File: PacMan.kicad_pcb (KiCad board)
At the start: 2 copper layers, 139.7 x 117.5 mm, 153 parts, among them J1 POWER+, J10 SEG2 CellMen, J11 SEG1 Balance, J12 SEG2 Balance, J13 AIR Left, J14 AIR Right, J15 SEG1, J16 SEG2, J2 POWER-, J3 TSV IN, J4 Charge Detection, J5 SEG1 CellMen, J6 BusBar Current Sensor, J7 Panel, J8 SLOOP, J9 GLV/CAN, K1 G5Q-1A4 DC24, K2 T9AS1D12-24, K3 T9AS1D12-24, Q1 BSS123, Q2 DMN3730U, Q4 DMP10H4D2S, Q5 DMP10H4D2S, U1 MCP9804, U10 LTC4151, U11 INA592, U12 VIFSD1-S24-S5-SIP, U13 V7805-500, U14 Si8600AC, U15 Si8600AC, U16 TEC3-2419, U17 TEC3-2419, U18 AP2204K-5.0, U19 INA233, U2 TEC2-4815WI, U20 INA233, U3 ADM6320, U4 MCP2551-I-SN, U5 ESP32_DEVKITC, U6 MCP23008, U7 BQ32002, U8 ACHS-7122, U9 PDQE10-Q48-S24-D, Y1 RTC_32K

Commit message: Re-layout to account for the new esp32, put on the RTC, the balancing measurement stuff, pretty much finished up the board, added some comments to schematic and other changes
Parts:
- removed TP1: TSV_RTN, Resistor_SMD:R_0805_2012Metric_Pad1.15x1.40mm_HandSolder
- removed TP2: TSV_5V, TestPoint:TestPoint_Pad_D1.5mm
- C24, C25, C26: footprint Capacitor_SMD:C_0805_2012Metric_Pad1.15x1.40mm_HandSolder -> Capacitor_SMD:C_1206_3216Metric_Pad1.42x1.75mm_HandSolder
- C27: value 4.7uF -> 4.7uF/50V; footprint Capacitor_SMD:C_0805_2012Metric_Pad1.15x1.40mm_HandSolder -> Capacitor_SMD:C_1206_3216Metric_Pad1.42x1.75mm_HandSolder
- C30: value 1u -> 1u/50V
- C32: value 2.2u -> 2.2u/25V
- F1: value Pack+ -> 500mA
- F2: value Pack- -> 500mA
- J11: value SEG1 Balance -> BAL1
- J12: value SEG2 Balance -> BAL2
- Q1: value BSS123 -> DMN3730U
- U12: value VIFSD1-S24-S5-SIP -> MEF1S2405SP3C
- Y1: footprint Crystal:Crystal_SMD_SeikoEpson_MC405-2Pin_9.6x4.1mm_HandSoldering -> Crystal:Crystal_SMD_SeikoEpson_MC405-2Pin_9.6x4.1mm
- moved D7 171.9 mm to (203.2, 106.7), turned to 270 degrees
- moved R41 170.3 mm to (200.7, 106.7), turned to 270 degrees
- moved Q2 162.2 mm to (197.5, 106.7)
- moved Y1 142.5 mm to (116.8, 117.5), turned to 180 degrees
- moved BT1 138.2 mm to (113.7, 124.5), turned to 180 degrees
- moved C34 130.3 mm to (120.7, 127.0), turned to 180 degrees
- moved U7 112.3 mm to (120.7, 123.2)
- moved U5 56.6 mm to (142.9, 130.8)
- moved U20 43.5 mm to (94.6, 49.5), turned to 90 degrees
- moved R37 42.5 mm to (94.6, 42.5), turned to 0 degrees
- moved U19 40.8 mm to (111.1, 49.5), turned to 90 degrees
- moved R36 38.1 mm to (111.1, 42.5), turned to 0 degrees
- moved LOGO2 37.5 mm to (158.1, 40.6)
- moved LOGO1 36.8 mm to (142.9, 43.2)
- moved C33 36.7 mm to (90.8, 52.1)
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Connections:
- net /TSV_5V_AMPS renamed /AMPS_PWR
- C14 pad 2: /PACK_RTN -> /BAL_SEG1-
- C16 pad 1: /PACK_RTN -> /BAL_SEG1-
- C17 pad 2: /PACK_RTN -> /BAL_SEG1-
- C20 pad 2: /SEG2_RTN -> /BAL_SEG2-
- C23 pad 2: /PACK_RTN -> /BAL_SEG1-
- C27 pad 2: /PACK_RTN -> /BAL_SEG1-
- C28 pad 2: /PACK_RTN -> /BAL_SEG1-
- C29 pad 2: /SEG2_RTN -> /BAL_SEG2-
- C30 pad 2: /SEG2_RTN -> /BAL_SEG2-
- C31 pad 1: /PACK_RTN -> /BAL_SEG1-
- C32 pad 2: /SEG2_RTN -> /BAL_SEG2-
- C33 pad 1: /SEG2_RTN -> /BAL_SEG2-
- F2 pad 2: /PACK_RTN -> /BAL_SEG1-
- ISO4 pad 3: /PACK_RTN -> /BAL_SEG1-
- J10 pad 2: /SEG2_RTN -> /BAL_SEG2-
- J10 pad 5: /SEG2_RTN -> /BAL_SEG2-
- J11 pad 1: (no net) -> /BAL_SEG1-
- J11 pad 2: (no net) -> /BAL_SEG1+
- J12 pad 1: (no net) -> /BAL_SEG2-
- J12 pad 2: (no net) -> /BAL_SEG2+
- J15 pad 1: (no net) -> /BAL_SEG1-
- J15 pad 2: (no net) -> /SEG1+
- J16 pad 1: (no net) -> /BAL_SEG2-
- J16 pad 2: (no net) -> /SEG2+
- J5 pad 2: /PACK_RTN -> /BAL_SEG1-
- J5 pad 5: /PACK_RTN -> /BAL_SEG1-
- J6 pad 4: /PACK_RTN -> /BAL_SEG1-
- J7 pad 11: /DISP_BUSY -> /DISP_CS
- J7 pad 13: /DISP_DC -> /DISP_BUSY
- J7 pad 17: /DISP_CS -> /DISP_DC
- R30 pad 1: /PACK_RTN -> /BAL_SEG1-
- R31 pad 1: /PACK_RTN -> /BAL_SEG1-
- R34 pad 2: /PACK_RTN -> /BAL_SEG1-
- R36 pad 1: /Charging/SEG1+ -> /SEG1+
- R36 pad 2: /Charging/BAL_SEG1+ -> /BAL_SEG1+
- R37 pad 1: /Charging/SEG2+ -> /SEG2+
- R37 pad 2: /Charging/BAL_SEG2+ -> /BAL_SEG2+
- TP14 pad 1: /SEG2_RTN -> /BAL_SEG2-
- U10 pad 3: /PACK_RTN -> /BAL_SEG1-
- U10 pad 4: /PACK_RTN -> /BAL_SEG1-
- U10 pad 9: /PACK_RTN -> /BAL_SEG1-
- U11 pad 1: /PACK_RTN -> /BAL_SEG1-
- U11 pad 4: /PACK_RTN -> /BAL_SEG1-
- U12 pad 4: /PACK_RTN -> /BAL_SEG1-
- U14 pad 5: /PACK_RTN -> /BAL_SEG1-
- U15 pad 5: /SEG2_RTN -> /BAL_SEG2-
- U16 pad 7: /PACK_RTN -> /BAL_SEG1-
- U17 pad 7: /SEG2_RTN -> /BAL_SEG2-
- U18 pad 2: /SEG2_RTN -> /BAL_SEG2-
- U19 pad 1: /PACK_RTN -> /BAL_SEG1-
- U19 pad 10: /Charging/BAL_SEG1+ -> /BAL_SEG1+
- U19 pad 2: /PACK_RTN -> /BAL_SEG1-
- U19 pad 7: /PACK_RTN -> /BAL_SEG1-
- U19 pad 8: /Charging/BAL_SEG1+ -> /BAL_SEG1+
- U19 pad 9: /Charging/SEG1+ -> /SEG1+
- U20 pad 1: /SEG2_RTN -> /BAL_SEG2-
- U20 pad 10: /Charging/BAL_SEG2+ -> /BAL_SEG2+
- U20 pad 2: /SEG2_RTN -> /BAL_SEG2-
- U20 pad 7: /SEG2_RTN -> /BAL_SEG2-
- U20 pad 8: /Charging/BAL_SEG2+ -> /BAL_SEG2+
- U20 pad 9: /Charging/SEG2+ -> /SEG2+
- U5 pad 21: (no net) -> /MCU/WATCHDOG
- U5 pad 29: /DISP_BUSY -> (no net)
- U5 pad 3: /MCU/BTN_CENTER_MCU -> /MCU/BTN_LEFT_MCU
- U5 pad 30: /~CHRG_DETECT -> (no net)
- U5 pad 31: /MCU/WATCHDOG -> /DISP_BUSY
- U5 pad 33: (no net) -> /~CHRG_DETECT
- U5 pad 4: /MCU/BTN_UP_MCU -> /MCU/BTN_RIGHT_MCU
- U5 pad 5: /MCU/BTN_DOWN_MCU -> /MCU/BTN_UP_MCU
- U5 pad 6: /MCU/BTN_LEFT_MCU -> /MCU/BTN_DOWN_MCU
- U5 pad 7: /MCU/BTN_RIGHT_MCU -> /MCU/BTN_CENTER_MCU
- U9 pad 1: /PACK_RTN -> /BAL_SEG1-
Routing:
- net /SEG1_5V: track 182.5 -> 227.5 mm
- net /MCU/WATCHDOG: track 81.8 -> 44.8 mm, vias 5 -> 2
- net /BAL_SEG1-: track 0.00 -> 36.2 mm, vias 0 -> 22
- net /LV_3V3: track 277.3 -> 311.1 mm, vias 15 -> 16
- net /LV_24V: track 195.4 -> 226.1 mm
- net /CHRG_EN: track 50.2 -> 20.5 mm
- net /SEG2_5V: track 37.1 -> 65.3 mm
- net /PACK_RTN: track 24.2 -> 0.00 mm, vias 22 -> 0
- net /DISP_CS: track 44.9 -> 60.3 mm, vias 0 -> 2
- net /CHRG_LED: track 68.7 -> 82.5 mm
- net /PACK_FUSED: track 21.3 -> 34.7 mm
- net /BAL_SEG2-: track 0.00 -> 12.8 mm, vias 0 -> 2
- net /BAL_SEG2+: track 0.00 -> 11.6 mm
- net /BAL_SEG1+: track 0.00 -> 11.5 mm
- net /MCU/CANTX: track 38.8 -> 50.3 mm
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- added copper zone on B.Cu, net /BAL_SEG1-
- added copper zone on F.Cu, net /BAL_SEG1-
- added copper zone on B.Cu, net /BAL_SEG2-
- removed copper zone on B.Cu, net /PACK_RTN
- removed copper zone on F.Cu, net /PACK_RTN
- removed copper zone on B.Cu, net /SEG2_RTN
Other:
- board size 139.7 x 117.5 mm -> 139.7 x 114.3 mm
- board text added: "Charging Enabled"

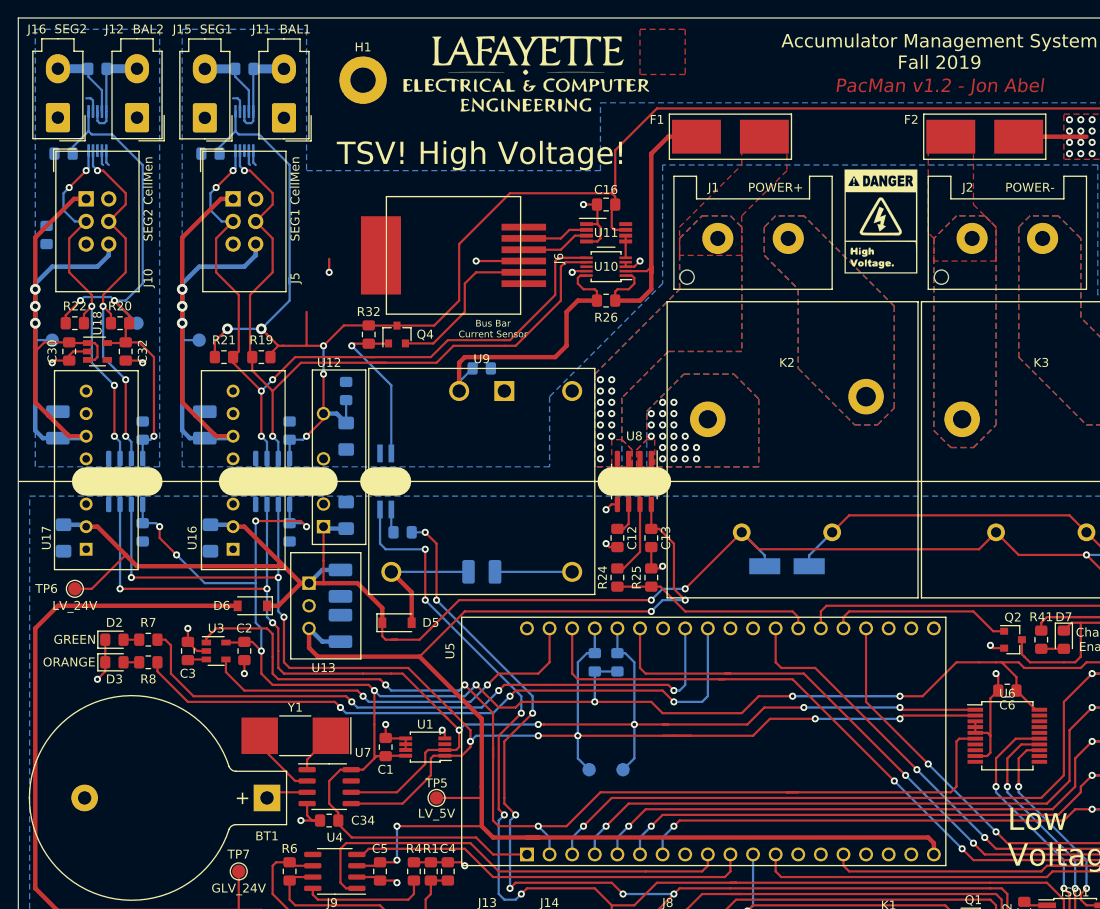
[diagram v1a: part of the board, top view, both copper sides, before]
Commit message: switched some ESP32 pins around, hopefully fixed some grounding stuff, cleaned up schematic naming slightly
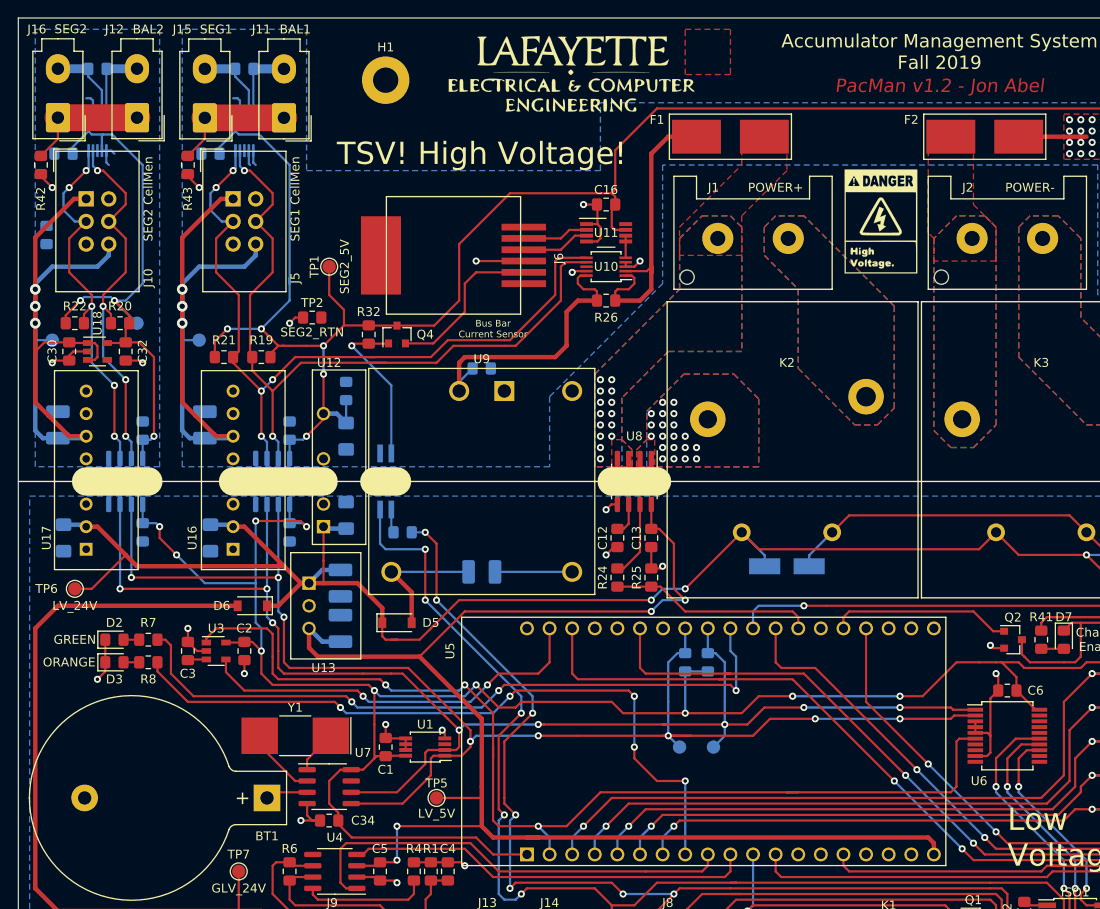
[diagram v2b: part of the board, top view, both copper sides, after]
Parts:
- added R42: 10k, Resistor_SMD:R_0805_2012Metric_Pad1.15x1.40mm_HandSolder, F.Cu at (88.3, 53.3)
- added R43: 10k, Resistor_SMD:R_0805_2012Metric_Pad1.15x1.40mm_HandSolder, F.Cu at (104.8, 53.3)
- added TP1: SEG2_5V, TestPoint:TestPoint_Pad_D1.5mm, F.Cu at (120.7, 64.8)
- added TP2: SEG2_RTN, Resistor_SMD:R_0805_2012Metric_Pad1.15x1.40mm_HandSolder, F.Cu at (118.7, 70.5)
- moved TP9 10.5 mm to (163.8, 118.7)
- moved TP8 10.5 mm to (160.0, 118.7)
- moved R23 10.2 mm to (160.7, 109.2)
- moved R27 10.2 mm to (163.2, 109.2)
- moved LOGO1 5.08 mm to (148.0, 43.2)
- moved LOGO2 5.08 mm to (163.2, 40.6)
- moved H1 2.54 mm to (127.0, 43.8)
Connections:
- C14 pad 2: /BAL_SEG1- -> /SEG1_RTN
- C16 pad 1: /BAL_SEG1- -> /SEG1_RTN
- C17 pad 2: /BAL_SEG1- -> /SEG1_RTN
- C20 pad 2: /BAL_SEG2- -> /SEG2_RTN
- C23 pad 2: /BAL_SEG1- -> /SEG1_RTN
- C27 pad 2: /BAL_SEG1- -> /SEG1_RTN
- C28 pad 2: /BAL_SEG1- -> /SEG1_RTN
- C29 pad 2: /BAL_SEG2- -> /SEG2_RTN
- C30 pad 2: /BAL_SEG2- -> /SEG2_RTN
- C31 pad 1: /BAL_SEG1- -> /SEG1_RTN
- C32 pad 2: /BAL_SEG2- -> /SEG2_RTN
- C33 pad 1: /BAL_SEG2- -> /SEG2_RTN
- F2 pad 2: /BAL_SEG1- -> /SEG1_RTN
- ISO4 pad 3: /BAL_SEG1- -> /SEG1_RTN
- J10 pad 2: /BAL_SEG2- -> /SEG2_RTN
- J10 pad 5: /BAL_SEG2- -> /SEG2_RTN
- J5 pad 2: /BAL_SEG1- -> /SEG1_RTN
- J5 pad 5: /BAL_SEG1- -> /SEG1_RTN
- J6 pad 4: /BAL_SEG1- -> /SEG1_RTN
- R30 pad 1: /BAL_SEG1- -> /SEG1_RTN
- R31 pad 1: /BAL_SEG1- -> /SEG1_RTN
- R34 pad 2: /BAL_SEG1- -> /SEG1_RTN
- TP14 pad 1: /BAL_SEG2- -> /SEG2_RTN
- U10 pad 3: /BAL_SEG1- -> /SEG1_RTN
- U10 pad 4: /BAL_SEG1- -> /SEG1_RTN
- U10 pad 9: /BAL_SEG1- -> /SEG1_RTN
- U11 pad 1: /BAL_SEG1- -> /SEG1_RTN
- U11 pad 4: /BAL_SEG1- -> /SEG1_RTN
- U12 pad 4: /BAL_SEG1- -> /SEG1_RTN
- U14 pad 5: /BAL_SEG1- -> /SEG1_RTN
- U15 pad 5: /BAL_SEG2- -> /SEG2_RTN
- U16 pad 7: /BAL_SEG1- -> /SEG1_RTN
- U17 pad 7: /BAL_SEG2- -> /SEG2_RTN
- U18 pad 2: /BAL_SEG2- -> /SEG2_RTN
- U19 pad 1: /BAL_SEG1- -> /SEG1_RTN
- U19 pad 2: /BAL_SEG1- -> /SEG1_RTN
- U19 pad 7: /BAL_SEG1- -> /SEG1_RTN
- U20 pad 1: /BAL_SEG2- -> /SEG2_RTN
- U20 pad 2: /BAL_SEG2- -> /SEG2_5V
- U20 pad 7: /BAL_SEG2- -> /SEG2_RTN
- U5 pad 23: /SDA_GLV -> (no net)
- U5 pad 24: /SCL_GLV -> (no net)
- U5 pad 27: /MCU/LED1 -> /SDA_GLV
- U5 pad 28: /MCU/LED2 -> /SCL_GLV
- U5 pad 29: (no net) -> /MCU/LED1
- U5 pad 30: (no net) -> /~CHRG_DETECT
- U5 pad 33: /~CHRG_DETECT -> (no net)
- U5 pad 8: (no net) -> /MCU/LED2
- U9 pad 1: /BAL_SEG1- -> /SEG1_RTN
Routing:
- net /SEG1_RTN: track 0.00 -> 38.5 mm, vias 0 -> 23
- net /BAL_SEG1-: track 36.2 -> 13.9 mm, vias 22 -> 0
- net /SEG2_RTN: track 0.00 -> 14.3 mm, vias 0 -> 3
- net /~CHRG_DETECT: track 49.8 -> 57.4 mm, vias 1 -> 2
- net /MCU/LED1: track 72.2 -> 78.6 mm
- net /MCU/LED2: track 74.3 -> 79.9 mm, vias 3 -> 5
- net /SEG1_5V: track 227.5 -> 231.0 mm
- net /SDA_GLV: track 165.6 -> 163.1 mm
- net /SCL_GLV: track 163.4 -> 160.9 mm
- net /SEG2_5V: track 65.3 -> 67.2 mm
- net /LV_3V3: track 311.1 -> 312.4 mm
- net /BAL_SEG2-: track 12.8 -> 14.0 mm, vias 2 -> 0
- added copper zone on B.Cu, net /SEG1_RTN
- added copper zone on F.Cu, net /SEG1_RTN
- added copper zone on B.Cu, net /SEG2_RTN
- removed copper zone on B.Cu, net /BAL_SEG1-
- removed copper zone on F.Cu, net /BAL_SEG1-
- removed copper zone on B.Cu, net /BAL_SEG2-

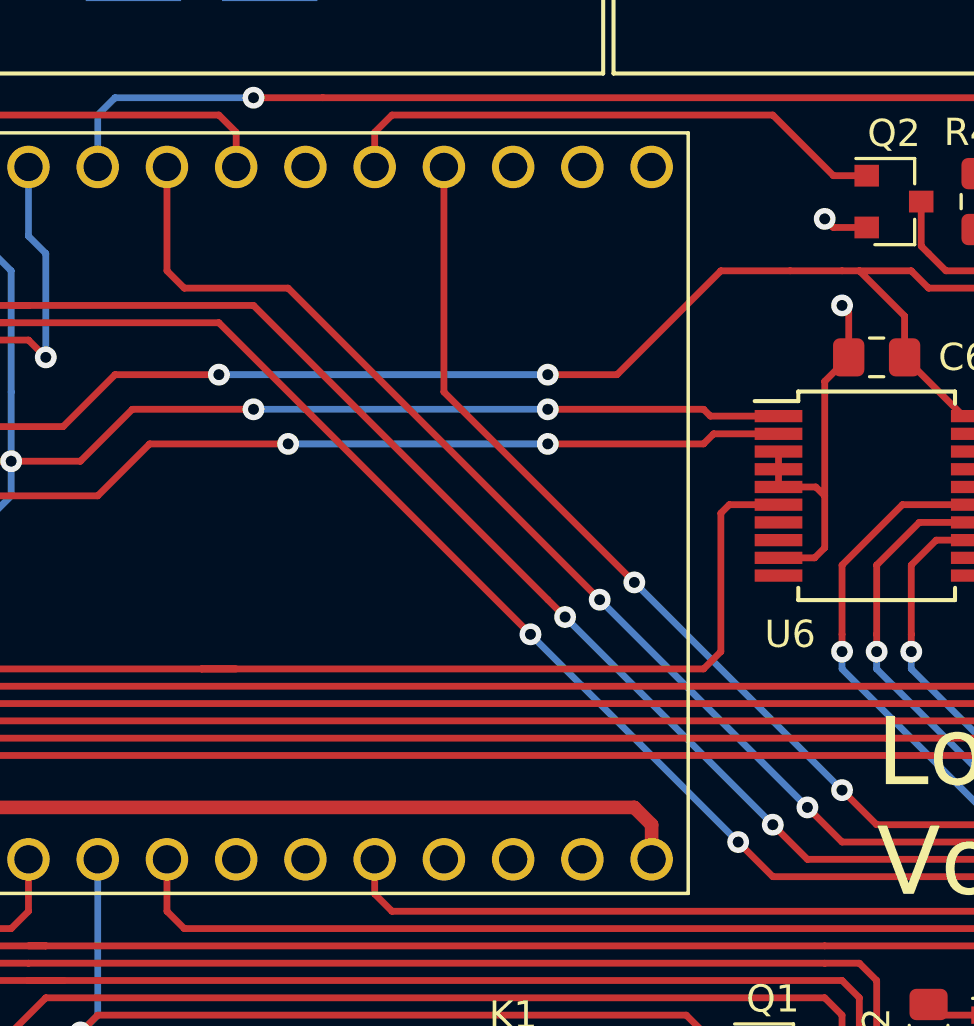
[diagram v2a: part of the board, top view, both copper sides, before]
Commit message: Added connection to IO expander interrupt pin
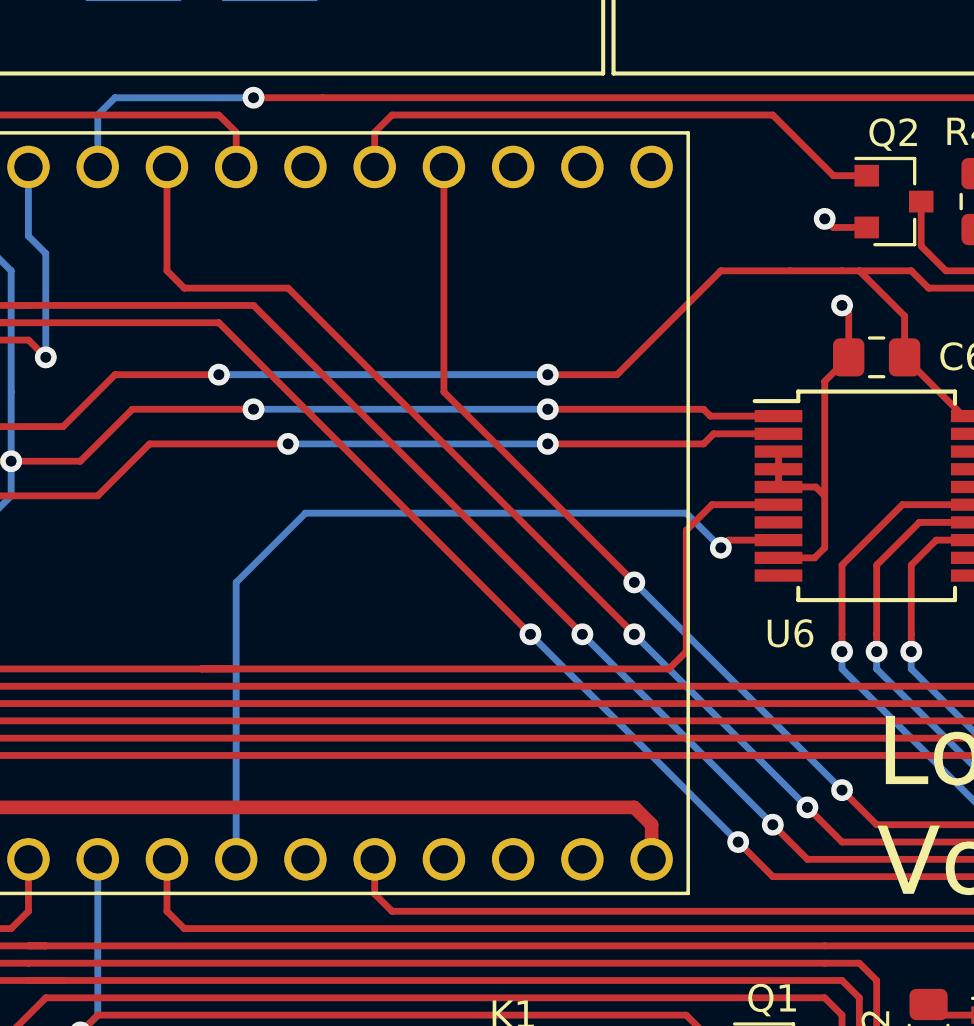
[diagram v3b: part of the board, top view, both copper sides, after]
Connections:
- H1 pad 1: (no net) -> Net-(H1-Pad1)
- H2 pad 1: (no net) -> Net-(H2-Pad1)
- J6 pad 1: (no net) -> Net-(J6-Pad1)
- J6 pad 6: (no net) -> Net-(J6-Pad6)
- U1 pad 3: (no net) -> Net-(U1-Pad3)
- U10 pad 8: (no net) -> Net-(U10-Pad8)
- U11 pad 8: (no net) -> Net-(U11-Pad8)
- U16 pad 3: (no net) -> Net-(U16-Pad3)
- U17 pad 3: (no net) -> Net-(U17-Pad3)
- U18 pad 4: (no net) -> Net-(U18-Pad4)
- U19 pad 3: (no net) -> Net-(U19-Pad3)
- U2 pad 3: (no net) -> Net-(U2-Pad3)
- U20 pad 3: (no net) -> Net-(U20-Pad3)
- U4 pad 5: (no net) -> Net-(U4-Pad5)
- U5 pad 13: (no net) -> /MCU/IO_INT
- U5 pad 16: (no net) -> Net-(U5-Pad16)
- U5 pad 17: (no net) -> Net-(U5-Pad17)
- U5 pad 18: (no net) -> Net-(U5-Pad18)
- U5 pad 23: (no net) -> Net-(U5-Pad23)
- U5 pad 24: (no net) -> Net-(U5-Pad24)
- U5 pad 33: (no net) -> Net-(U5-Pad33)
- U5 pad 36: (no net) -> Net-(U5-Pad36)
- U5 pad 37: (no net) -> Net-(U5-Pad37)
- U5 pad 38: (no net) -> Net-(U5-Pad38)
- U6 pad 10: (no net) -> Net-(U6-Pad10)
- U6 pad 11: (no net) -> Net-(U6-Pad11)
- U6 pad 12: (no net) -> Net-(U6-Pad12)
- U6 pad 16: (no net) -> Net-(U6-Pad16)
- U6 pad 17: (no net) -> Net-(U6-Pad17)
- U6 pad 18: (no net) -> Net-(U6-Pad18)
- U6 pad 19: (no net) -> Net-(U6-Pad19)
- U6 pad 7: (no net) -> Net-(U6-Pad7)
- U6 pad 8: (no net) -> /MCU/IO_INT
- U7 pad 7: (no net) -> Net-(U7-Pad7)
- U9 pad 6: (no net) -> Net-(U9-Pad6)
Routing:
- net /MCU/IO_INT: track 0.00 -> 31.7 mm, vias 0 -> 1
